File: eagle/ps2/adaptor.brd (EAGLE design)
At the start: 100 x 80 mm, 9 parts, among them T1 BSS138, T3 BSS138

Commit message: updated
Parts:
- moved JP2 36.8 mm to (12.7, 38.7)
- moved JP1 36.4 mm to (31.8, 45.7)
- moved R4 26.7 mm to (25.4, 52.7)
- moved R3 25.7 mm to (25.4, 43.2)
- moved T3 25.5 mm to (25.4, 48.3)
- moved HDR1 20.3 mm to (12.7, 48.3), turned to 270 degrees
- moved R2 5.12 mm to (19.1, 52.7)
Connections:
- net CLK_3V3: now also JP1.2; no longer JP1.1
- net DATA_3V3: now also JP1.1; no longer JP1.2
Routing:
- net GND: track 0.00 -> 47.1 mm
- net VCC_5V: track 0.00 -> 33.2 mm
- net DATA_5V: track 0.00 -> 23.6 mm
- net CLK_3V3: track 0.00 -> 22.1 mm
- net VCC_3V3: track 0.00 -> 17.2 mm
- net DATA_3V3: track 0.00 -> 9.63 mm
- net CLK_5V: track 0.00 -> 9.15 mm

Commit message: updated
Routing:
- net GND: track 47.1 -> 28.9 mm
- net CLK_3V3: track 22.1 -> 36.1 mm
- net VCC_5V: track 33.2 -> 46.0 mm
- net DATA_5V: track 23.6 -> 19.2 mm
- net DATA_3V3: track 9.63 -> 8.69 mm
- net VCC_3V3: track 17.2 -> 16.5 mm

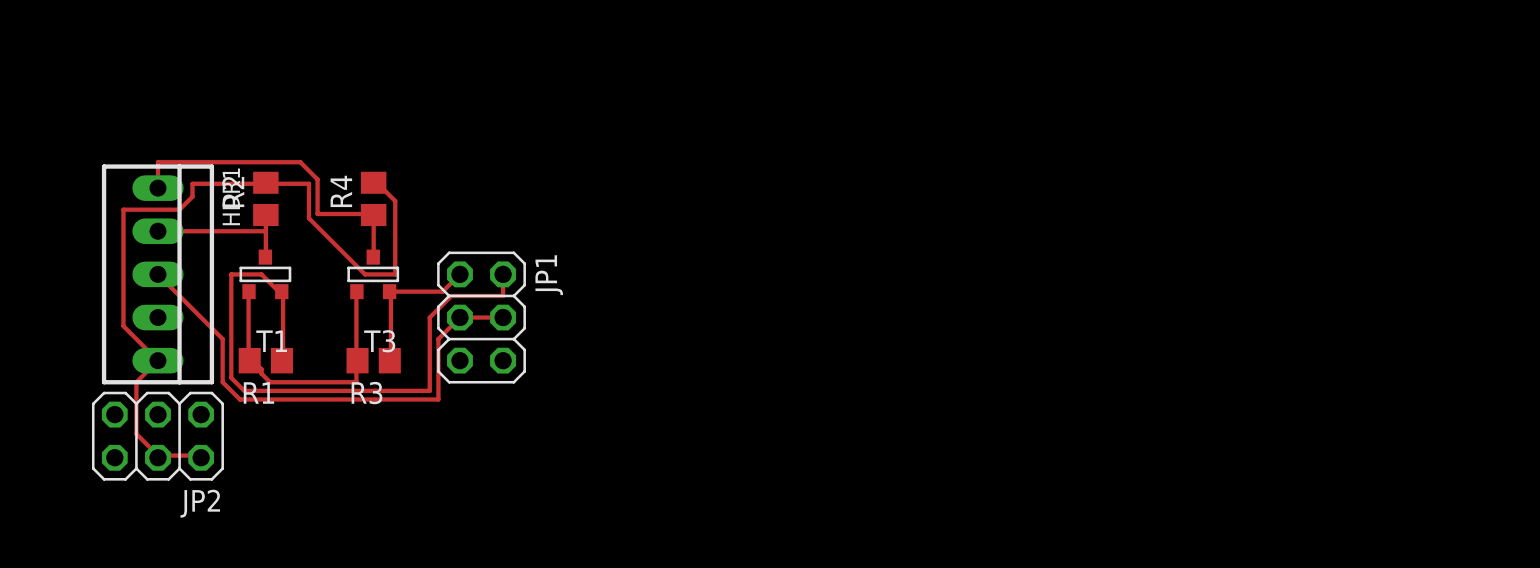
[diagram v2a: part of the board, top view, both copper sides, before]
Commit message: nicer connections
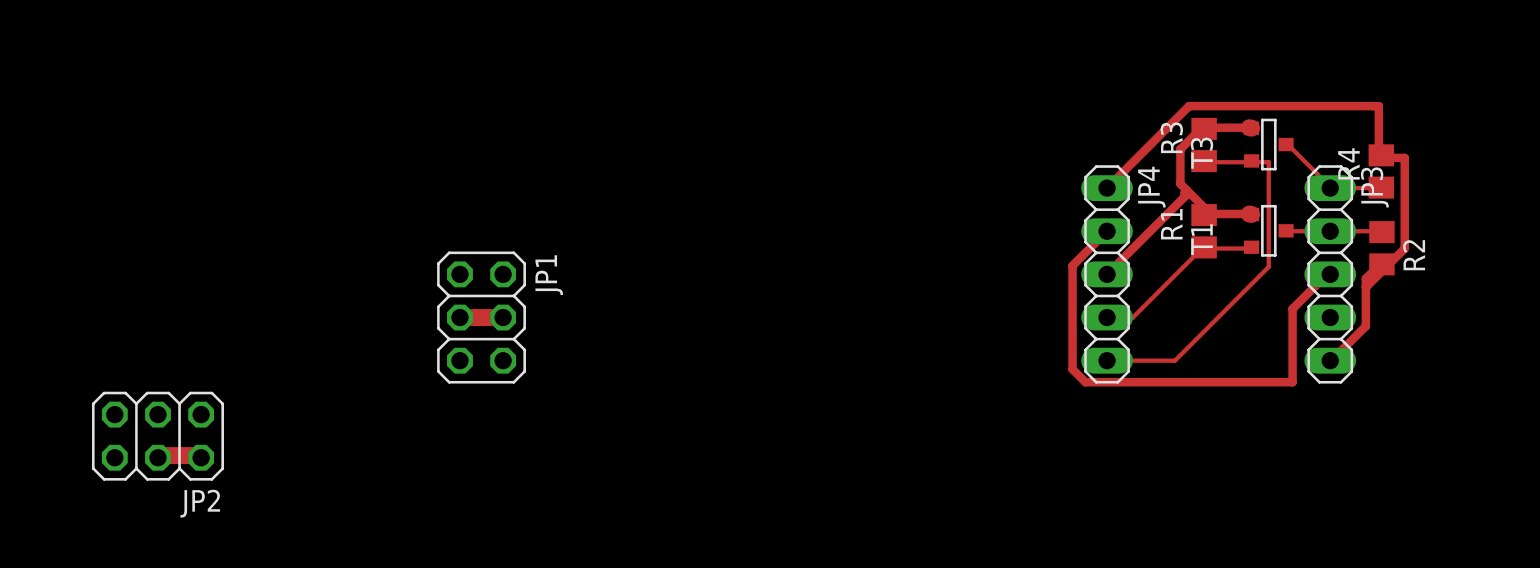
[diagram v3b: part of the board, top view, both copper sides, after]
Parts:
- removed HDR1: 22-23-2051, con-molex:22-23-2051
- added JP3: PS2, pinhead:1X05
- added JP4: signals, pinhead:1X05
- JP1: value (none) -> 3V3 signals
- JP2: value (none) -> 5V header
- moved R2 65.8 mm to (84.8, 49.8), turned to 270 degrees
- moved R4 59.3 mm to (84.7, 54.3)
- moved T1 59.1 mm to (78.1, 50.8), turned to 90 degrees
- moved R1 55.8 mm to (74.3, 50.8), turned to 90 degrees
- moved T3 53.3 mm to (78.1, 55.9), turned to 90 degrees
- moved R3 50.5 mm to (74.3, 55.9), turned to 90 degrees
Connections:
- new net X_CLK_3V3: JP1.2
- new net X_DATA_3V3: JP1.1
- new net X_GND: JP1.3, JP1.4
- new net X_VCC_5V: JP2.2, JP2.4
- net CLK_3V3: now also JP4.4; no longer JP1.2
- net CLK_5V: now also JP3.2; no longer HDR1.2
- net DATA_3V3: now also JP4.5; no longer JP1.1
- net DATA_5V: now also JP3.1; no longer HDR1.1
- net GND: now also JP3.3, JP4.2; no longer HDR1.3, JP1.3, JP1.4
- net VCC_3V3: now also JP4.3
- net VCC_5V: now also JP3.5, JP4.1; no longer HDR1.5, JP2.2, JP2.4
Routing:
- net CLK_3V3: track 36.1 -> 10.2 mm
- net DATA_3V3: track 8.69 -> 21.8 mm
- net DATA_5V: track 19.2 -> 6.81 mm
- net VCC_5V: track 46.0 -> 38.0 mm
- net CLK_5V: track 8.85 -> 5.65 mm
- net X_VCC_5V: track 0.00 -> 2.79 mm
- net X_GND: track 0.00 -> 2.54 mm
- net VCC_3V3: track 16.5 -> 19.0 mm
- net GND: track 28.9 -> 29.6 mm

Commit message: changed pin order - nicer now :)
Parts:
- moved R4 3.30 mm to (81.9, 56.1), turned to 0 degrees
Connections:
- net GND: now also JP4.3; no longer JP4.2
- net VCC_3V3: now also JP4.2; no longer JP4.3
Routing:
- net VCC_5V: track 38.0 -> 35.2 mm
- net GND: track 29.6 -> 27.1 mm
- net DATA_5V: track 6.81 -> 5.15 mm
- net VCC_3V3: track 19.0 -> 18.3 mm
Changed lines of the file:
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@@
 </element>
 <element name="R3" library="rcl" package="R0805" value="10K" x="74.295" y="55.88" rot="R90"/>
-<element name="R4" library="rcl" package="R0805" value="10K" x="84.725" y="54.32" rot="R90"/>
+<element name="R4" library="rcl" package="R0805" value="10K" x="81.925" y="56.06"/>
 <element name="JP1" library="pinhead" package="2X03" value="3V3 signals" x="31.75" y="45.72" rot="R270"/>
 <element name="JP2" library="pinhead" package="2X03" value="5V header" x="12.7" y="38.735" rot="R180"/>
@@
 <contactref element="R4" pad="1"/>
 <contactref element="JP3" pad="1"/>
-<wire x1="81.534" y1="53.594" x2="79.248" y2="55.88" width="0.254" layer="1"/>
+<wire x1="81.534" y1="53.594" x2="80.01" y2="55.118" width="0.254" layer="1"/>
+<wire x1="80.01" y1="55.118" x2="79.248" y2="55.88" width="0.254" layer="1"/>
 <wire x1="81.534" y1="53.34" x2="81.534" y2="53.594" width="0.254" layer="1"/>
 <wire x1="79.248" y1="55.88" x2="79.121" y2="55.9054" width="0.254" layer="1"/>
 <wire x1="81.534" y1="53.34" x2="81.72" y2="53.34" width="0.254" layer="1"/>
-<wire x1="81.72" y1="53.34" x2="84.582" y2="53.34" width="0.254" layer="1"/>
-<wire x1="84.582" y1="53.34" x2="84.725" y2="53.37" width="0.254" layer="1"/>
+<wire x1="80.01" y1="55.118" x2="80.772" y2="55.88" width="0.254" layer="1"/>
+<wire x1="80.772" y1="55.88" x2="80.975" y2="56.06" width="0.254" layer="1"/>
 </signal>
 <signal name="CLK_5V">
@@
 <contactref element="T3" pad="3"/>
 <contactref element="R3" pad="2"/>
-<contactref element="JP4" pad="3"/>
 <wire x1="76.962" y1="51.816" x2="77.089" y2="51.7906" width="1" layer="1"/>
 <wire x1="76.962" y1="56.896" x2="77.089" y2="56.8706" width="1" layer="1"/>
@@
 <wire x1="74.422" y1="51.816" x2="76.962" y2="51.816" width="0.5" layer="1"/>
 <wire x1="74.422" y1="51.816" x2="74.295" y2="51.75" width="0.5" layer="1"/>
+<contactref element="JP4" pad="2"/>
+<wire x1="68.58" y1="51.562" x2="72.898" y2="51.562" width="0.5" layer="1"/>
+<wire x1="72.898" y1="51.562" x2="74.168" y2="51.562" width="0.5" layer="1"/>
+<wire x1="68.58" y1="50.8" x2="68.58" y2="51.562" width="0.5" layer="1"/>
+<wire x1="74.168" y1="51.562" x2="74.295" y2="51.75" width="0.5" layer="1"/>
 <wire x1="72.898" y1="55.626" x2="73.914" y2="56.642" width="0.5" layer="1"/>
-<wire x1="72.898" y1="53.594" x2="72.898" y2="55.626" width="0.5" layer="1"/>
-<wire x1="74.422" y1="52.07" x2="73.279" y2="53.213" width="0.5" layer="1"/>
-<wire x1="73.279" y1="53.213" x2="72.898" y2="53.594" width="0.5" layer="1"/>
+<wire x1="72.898" y1="51.562" x2="72.898" y2="55.626" width="0.5" layer="1"/>
 <wire x1="73.914" y1="56.642" x2="74.295" y2="56.83" width="0.5" layer="1"/>
-<wire x1="74.422" y1="52.07" x2="74.295" y2="51.75" width="0.5" layer="1"/>
-<wire x1="73.152" y1="52.832" x2="68.58" y2="48.26" width="0.5" layer="1"/>
-<wire x1="73.152" y1="53.086" x2="73.152" y2="52.832" width="0.5" layer="1"/>
-<wire x1="73.152" y1="53.086" x2="73.279" y2="53.213" width="0.5" layer="1"/>
 </signal>
 <signal name="CLK_3V3">
@@
 <contactref element="JP3" pad="5"/>
 <contactref element="JP4" pad="1"/>
+<wire x1="73.406" y1="58.166" x2="68.58" y2="53.34" width="0.5" layer="1"/>
+<wire x1="82.804" y1="58.166" x2="73.406" y2="58.166" width="0.5" layer="1"/>
+<wire x1="82.804" y1="56.134" x2="82.804" y2="58.166" width="0.5" layer="1"/>
+<wire x1="82.804" y1="56.134" x2="82.875" y2="56.06" width="0.5" layer="1"/>
 <wire x1="83.82" y1="48.006" x2="84.582" y2="48.768" width="0.5" layer="1"/>
-<wire x1="83.82" y1="45.212" x2="83.82" y2="47.498" width="0.5" layer="1"/>
-<wire x1="83.82" y1="47.498" x2="83.82" y2="48.006" width="0.5" layer="1"/>
+<wire x1="83.82" y1="45.212" x2="83.82" y2="48.006" width="0.5" layer="1"/>
 <wire x1="81.788" y1="43.18" x2="83.82" y2="45.212" width="0.5" layer="1"/>
 <wire x1="84.582" y1="48.768" x2="84.765" y2="48.85" width="0.5" layer="1"/>
 <wire x1="81.788" y1="43.18" x2="81.72" y2="43.18" width="0.5" layer="1"/>
-<wire x1="86.106" y1="55.118" x2="84.836" y2="55.118" width="0.5" layer="1"/>
-<wire x1="86.106" y1="49.784" x2="86.106" y2="55.118" width="0.5" layer="1"/>
-<wire x1="83.82" y1="47.498" x2="86.106" y2="49.784" width="0.5" layer="1"/>
-<wire x1="84.836" y1="55.118" x2="84.725" y2="55.27" width="0.5" layer="1"/>
-<wire x1="73.406" y1="58.166" x2="68.58" y2="53.34" width="0.5" layer="1"/>
-<wire x1="84.582" y1="58.166" x2="73.406" y2="58.166" width="0.5" layer="1"/>
-<wire x1="84.582" y1="55.372" x2="84.582" y2="58.166" width="0.5" layer="1"/>
-<wire x1="84.582" y1="55.372" x2="84.725" y2="55.27" width="0.5" layer="1"/>
+<wire x1="86.106" y1="49.022" x2="84.836" y2="49.022" width="0.5" layer="1"/>
+<wire x1="86.106" y1="52.832" x2="86.106" y2="49.022" width="0.5" layer="1"/>
+<wire x1="83.058" y1="55.88" x2="86.106" y2="52.832" width="0.5" layer="1"/>
+<wire x1="84.836" y1="49.022" x2="84.765" y2="48.85" width="0.5" layer="1"/>
+<wire x1="83.058" y1="55.88" x2="82.875" y2="56.06" width="0.5" layer="1"/>
 </signal>
 <signal name="DATA_3V3">
@@
 <signal name="GND" class="1">
 <contactref element="JP3" pad="3"/>
-<contactref element="JP4" pad="2"/>
-<wire x1="66.548" y1="48.768" x2="68.58" y2="50.8" width="0.5" layer="1"/>
-<wire x1="66.548" y1="42.672" x2="66.548" y2="48.768" width="0.5" layer="1"/>
+<contactref element="JP4" pad="3"/>
+<wire x1="66.548" y1="46.228" x2="68.58" y2="48.26" width="0.5" layer="1"/>
+<wire x1="66.548" y1="42.672" x2="66.548" y2="46.228" width="0.5" layer="1"/>
 <wire x1="67.31" y1="41.91" x2="66.548" y2="42.672" width="0.5" layer="1"/>
 <wire x1="79.502" y1="41.91" x2="67.31" y2="41.91" width="0.5" layer="1"/>

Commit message: layout fiddling
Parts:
- removed JP1: 3V3 signals, pinhead:2X03
- removed JP2: 5V header, pinhead:2X03
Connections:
- removed net X_CLK_3V3: JP1.2
- removed net X_DATA_3V3: JP1.1
- removed net X_GND: JP1.3, JP1.4
- removed net X_VCC_5V: JP2.2, JP2.4
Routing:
- net DATA_3V3: track 21.8 -> 25.2 mm
- net X_VCC_5V: track 2.79 -> 0.00 mm
- net X_GND: track 2.54 -> 0.00 mm
- net VCC_5V: track 35.2 -> 36.1 mm
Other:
- board text added: "PS/2"

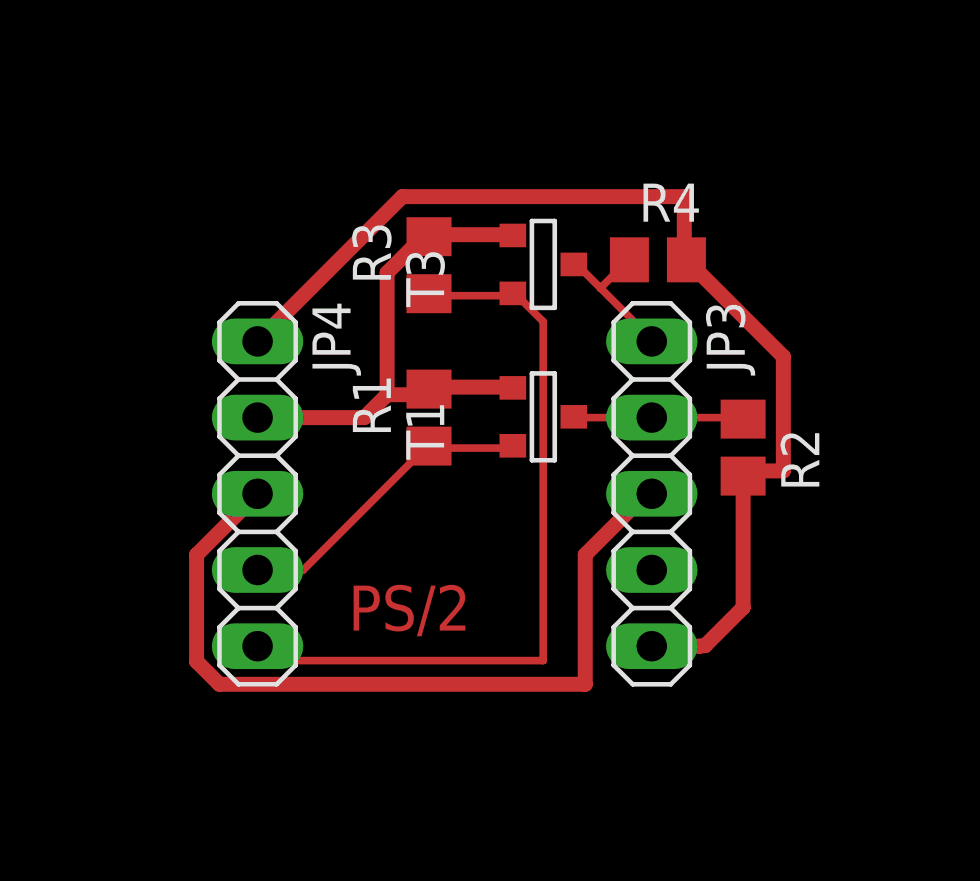
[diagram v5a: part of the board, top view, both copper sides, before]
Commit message: built ps2 adapter, updated docs to reflect pinout
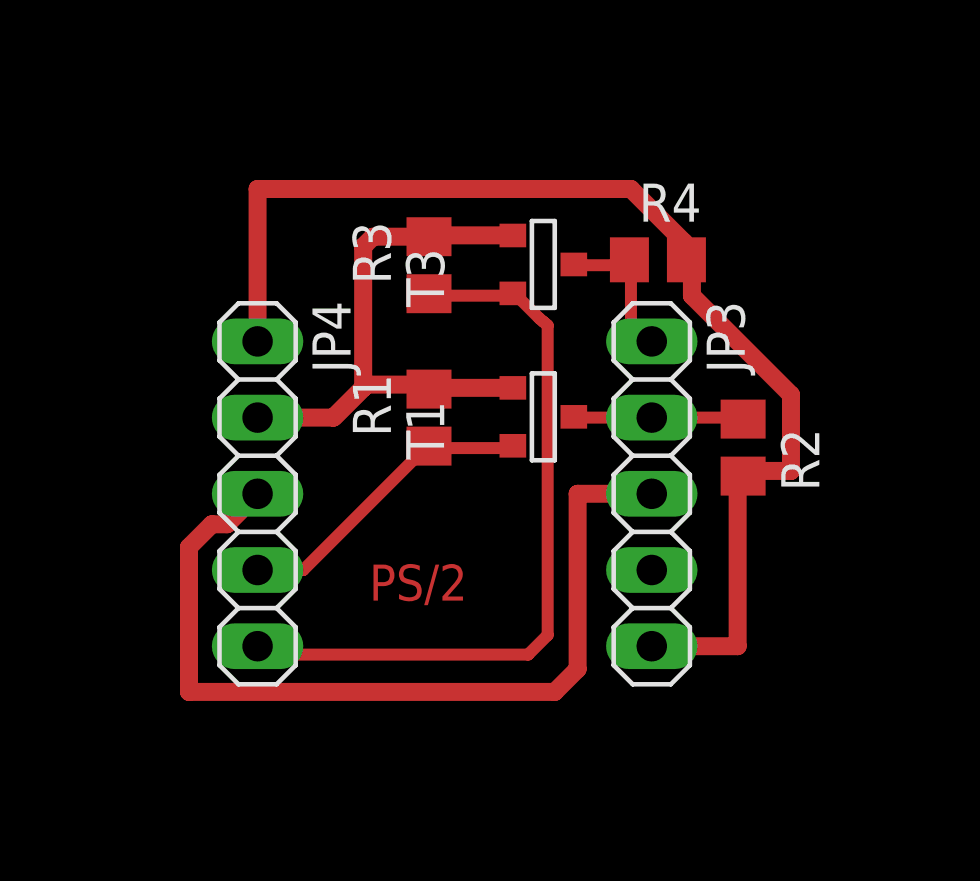
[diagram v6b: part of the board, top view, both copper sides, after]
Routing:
- net VCC_5V: track 36.1 -> 39.5 mm
- net VCC_3V3: track 17.8 -> 20.5 mm
- net GND: track 27.1 -> 29.4 mm
